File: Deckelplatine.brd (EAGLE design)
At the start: 110 x 75 mm, 69 parts, among them IC1 MAX1487EESA+, IC2 74HCT595D, IC3 74HCT595D, IC4 74HCT595D, IC5 74HCT595D, IC6 74HCT595D, J1 52808-2570, Q1 BC846BSMD, Q2 BC846BSMD, U1 LM2676S, X1 236-406/000-023, X2 233-502

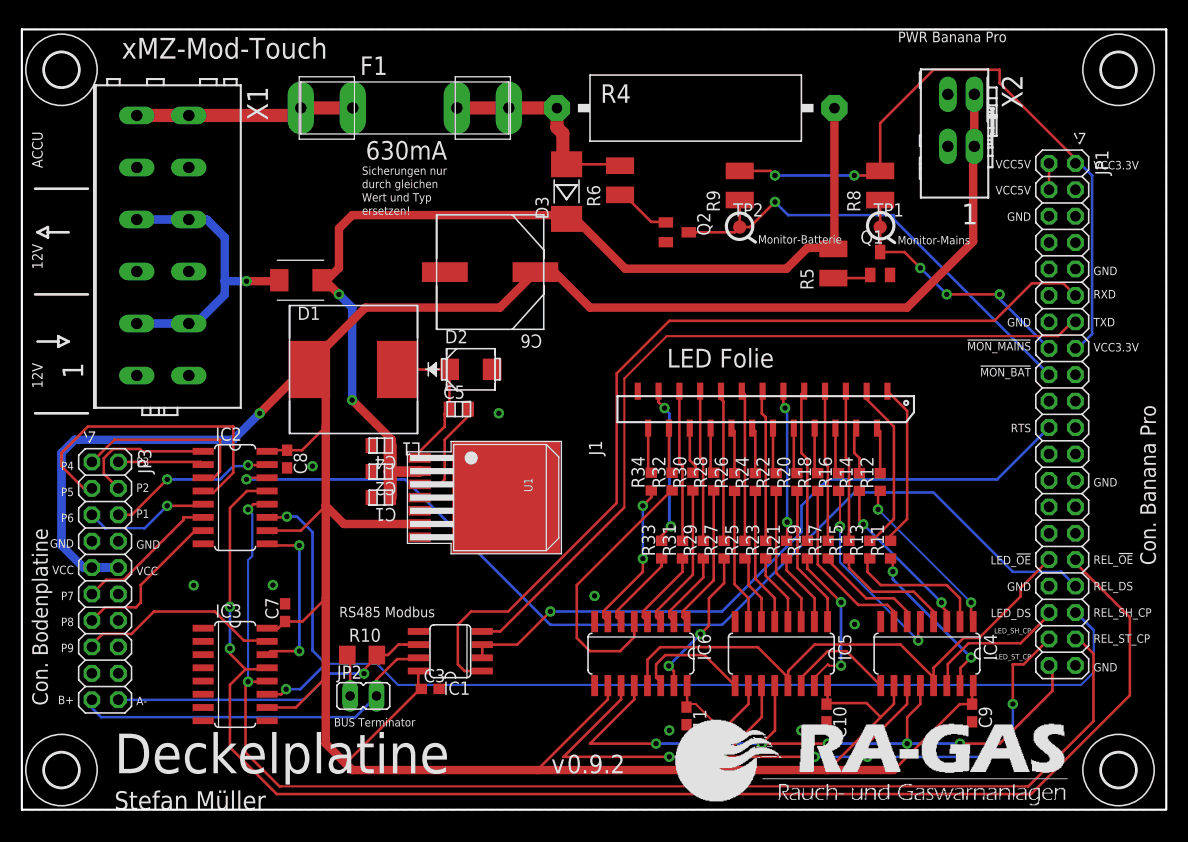
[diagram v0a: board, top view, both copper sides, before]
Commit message: Dateinamen umbenannt, die Versionsnummer wird in Git geführt
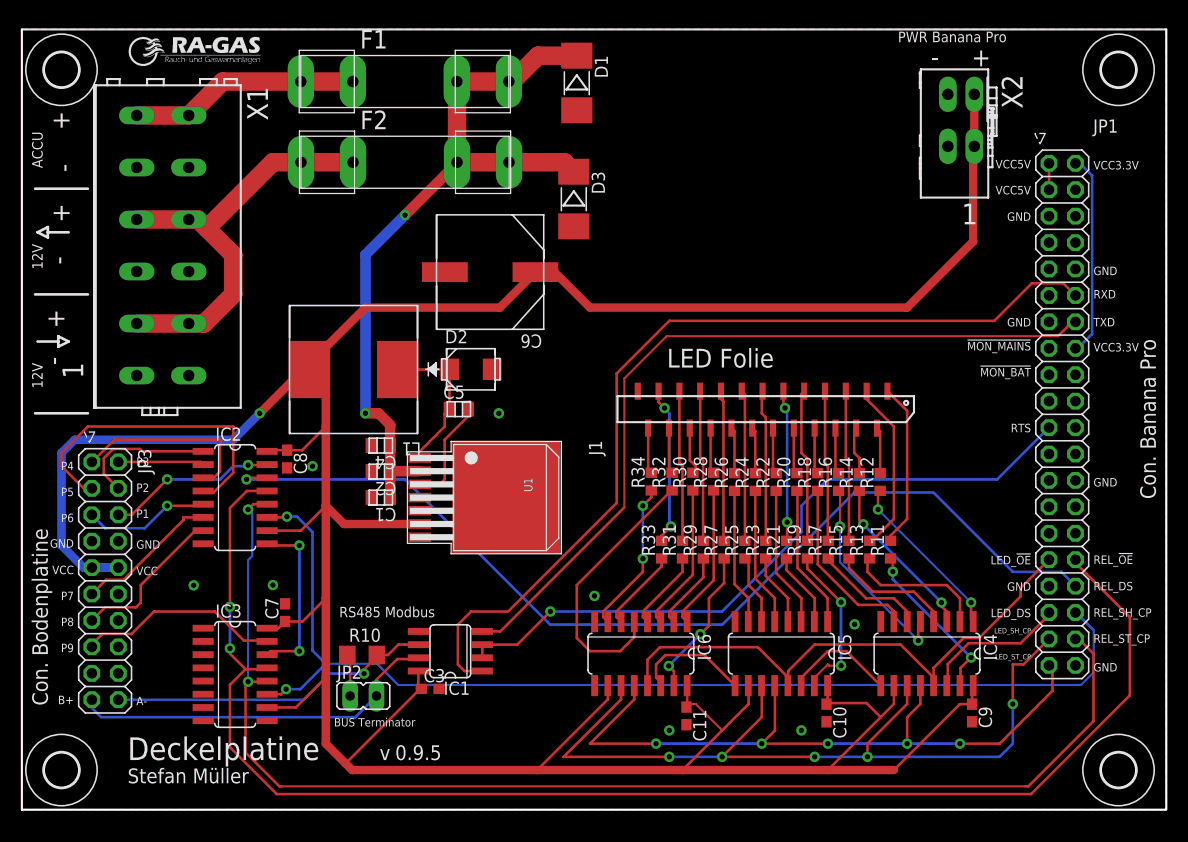
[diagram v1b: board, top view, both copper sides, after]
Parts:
- removed Q1, Q2: BC846BSMD, transistor-npn:SOT23
- removed R4: 150R, 4W, 5%, resistor-power:KH206-8
- removed R5, R6: 1k, rcl:R1210
- removed R8, R9: 10k, rcl:R1210
- removed TP1, TP2: TPSB1,27, testpad:B1,27
- added F2: 2AT, fuse-littlefuse:01110005MR
- D1: value SSB44 -> LL4005G; device diode:SMBJ -> diode:MELF-MLL41
- F1: value 01110005MR -> 0.63AT
- U$2: device xMZ-Mod-Touch-Bodenplatine:LOGO_RA-GAS -> xMZ-Mod-Touch-Bodenplatine:LOGO_RA-GAS-SMALL
- U$3: device xMZ-Mod-Touch-Bodenplatine:TEXT_NAME_VERSION_AUTHOR -> xMZ-Mod-Touch-Bodenplatine:TEXT_NAME_VERSION_AUTHOR-SMALL
- moved U$2 88.4 mm to (10.3, 71.5)
- moved D1 32.6 mm to (53.3, 69.8), turned to 270 degrees
- moved U$3 2.84 mm to (10.2, 2.54)
- moved F1 2.54 mm to (36.8, 70.0)
- moved D3 0.99 mm to (53.1, 58.7), turned to 270 degrees
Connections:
- removed net N$37: Q1.1, R5.1
- net !MON_BAT: no longer Q2.3, R9.1, TP2.TP
- net !MON_MAINS: no longer Q1.3, R8.1, TP1.TP
- net 12V_VIN: now also F2.1A, F2.1B; no longer C1.1, C2.1, C4.1, D1.A, D1.C, D3.C, R4.2, R5.2, U1.2
- net ACCU+: no longer D3.A, F1.2A, F1.2B, R4.1, R6.2
- net GND: now also D1.A, D3.A; no longer Q1.2, Q2.2
- net N$4: now also C1.1, C2.1, C4.1, D1.C, D3.C, F1.2A, F1.2B, F2.2A, F2.2B, U1.2; no longer Q2.1, R6.1
- net VCC3.3V: no longer R8.2, R9.2
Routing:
- net 12V_VIN: track 127.0 -> 41.6 mm, vias 3 -> 0
- net N$4: track 5.50 -> 72.4 mm, vias 0 -> 2
- net !MON_BAT: track 45.6 -> 0.00 mm, vias 1 -> 0
- net VCC3.3V: track 64.0 -> 19.5 mm, vias 2 -> 0
- net !MON_MAINS: track 25.3 -> 0.00 mm, vias 3 -> 0
- net ACCU+: track 41.7 -> 22.1 mm
- net N$37: track 3.69 -> 0.00 mm
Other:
- board text removed: "630mA"
- board text removed: "Monitor-Batterie"
- board text removed: "Monitor-Mains"
- board text removed: "Sicherungen nur durch gleichen Wert und Typ ersetzen!"
- board text removed: "xMZ-Mod-Touch"
